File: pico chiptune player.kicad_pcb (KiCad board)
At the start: 2 copper layers, 80 x 70.8 mm, 20 parts, among them J1 MicroSD, J2 Audio Out, SW1 Play / Pause, SW2 Next, SW3 Previous, U1 AY-3-8910, U2 0.96"OLED_I2C

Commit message: Refactor code structure for improved readability and maintainability
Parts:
- added G***: LOGO, LOGO, F.Cu at (120.5, 131.0)
- added G***: LOGO, LOGO, F.Cu at (148.9, 131.0)
- added G***: LOGO, LOGO, F.Cu at (173.0, 112.0)
- added G***: LOGO, LOGO, F.Cu at (177.3, 131.0)
- added G***: LOGO, LOGO, B.Cu at (148.9, 137.2)
- added G***: LOGO, LOGO, B.Cu at (120.2, 137.2)
- added G***: LOGO, LOGO, B.Cu at (177.2, 137.2)
- added R8: 10K, Resistor_SMD:R_0805_2012Metric_Pad1.20x1.40mm_HandSolder, B.Cu at (118.5, 88.5)
- added RV1: 3224W-1-103E, Potentiometer_SMD:Potentiometer_Bourns_3224W_Vertical, B.Cu at (116.5, 104.5)
- added U2: PAM8302AAS, Package_SO:SOIC-8_5.3x5.3mm_P1.27mm, B.Cu at (119.5, 95.0)
- C3: renamed from C4; value 10uF -> 1uF
- J2: value Audio Out -> Spk Out
- JP1: value SEL_TEST2 -> CLK DIV / 2; footprint Jumper:SolderJumper-3_P2.0mm_Open_TrianglePad1.0x1.5mm -> Jumper:SolderJumper-2_P1.3mm_Open_TrianglePad1.0x1.5mm
- R4: renamed from R3; value 1k -> 1K
- R5: renamed from R4; value 1k -> 1K
- R6: renamed from R5; value 1k -> 1K
- U1: value AY-3-8910 -> AY-3-8910 / YM2149F
- moved J2 26.2 mm to (123.5, 100.0), turned to 90 degrees
- moved C3 3.26 mm to (121.5, 83.5)
- moved SW1 2.51 mm to (145.6, 135.0)
- moved SW2 2.51 mm to (174.0, 135.0)
- moved SW3 2.51 mm to (117.2, 135.0)
- moved C2 1.62 mm to (116.0, 88.5), turned to -90 degrees
- moved JP1 0.71 mm to (118.3, 112.7), turned to 180 degrees
- moved C4 0.58 mm to (124.0, 107.5)
- renumbered C3 to C2, C1 to C4, C2 to C5, R7 to R2, R2 to R3, R6 to R7, U2 to U3
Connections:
- C3 pad 2: Net-(J2-Pin_2) -> Net-(C3-Pad2)
- J2 pad 1: GND -> Net-(J2-Pin_1)
- JP1 pad 1: +5V -> Net-(JP1-A)
- JP1 pad 2: Net-(JP1-C) -> GND
- U1 pad 26: Net-(JP1-C) -> Net-(JP1-A)
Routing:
- net Net-(C3-Pad2): track 0.00 -> 24.8 mm
- net +5V: track 163.2 -> 186.9 mm
- net Net-(U2-IN+): track 0.00 -> 11.8 mm
- net Net-(U2-~{SD}): track 0.00 -> 9.46 mm
- net Net-(JP1-C): track 8.24 -> 0.00 mm
- net Net-(JP1-A): track 0.00 -> 7.82 mm
- net Net-(C2-Pad1): track 16.4 -> 10.5 mm
- net Net-(J2-Pin_2): track 5.96 -> 11.8 mm
- net Net-(J2-Pin_1): track 0.00 -> 3.27 mm
- net /SW_PREV: track 36.0 -> 38.7 mm
- net /SW_PLAY: track 38.0 -> 39.6 mm
- net /SW_NEXT: track 51.7 -> 52.5 mm
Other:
- board text added: "+3.3V"
- board text added: "+5V"
- board text added: "/RESET"
- board text added: "A"
- board text added: "B"
- board text added: "C"
- board text added: "CD"
- board text added: "CLK"
- board text added: "CLK/2"
- board text added: "CND"
- board text added: "CS"
- board text added: "D0"
- board text added: "D1"
- board text added: "D2"
- board text added: "D3"
- board text added: "D4"
- board text added: "D5"
- board text added: "D6"
- board text added: "D7"
- board text added: "GND"
- board text added: "MISO"
- board text added: "MOSI"
- board text added: "RP2350 Pico 2 - AY-3-8910"
- board text added: "SCK"
- board text added: "SCL"
- board text added: "SDA"
- board text added: "Terence Ang / MotionFxDesign 2026"
- board text added: "VCC"
- board text added: "VOL"
- board text added: "terenceang.com"

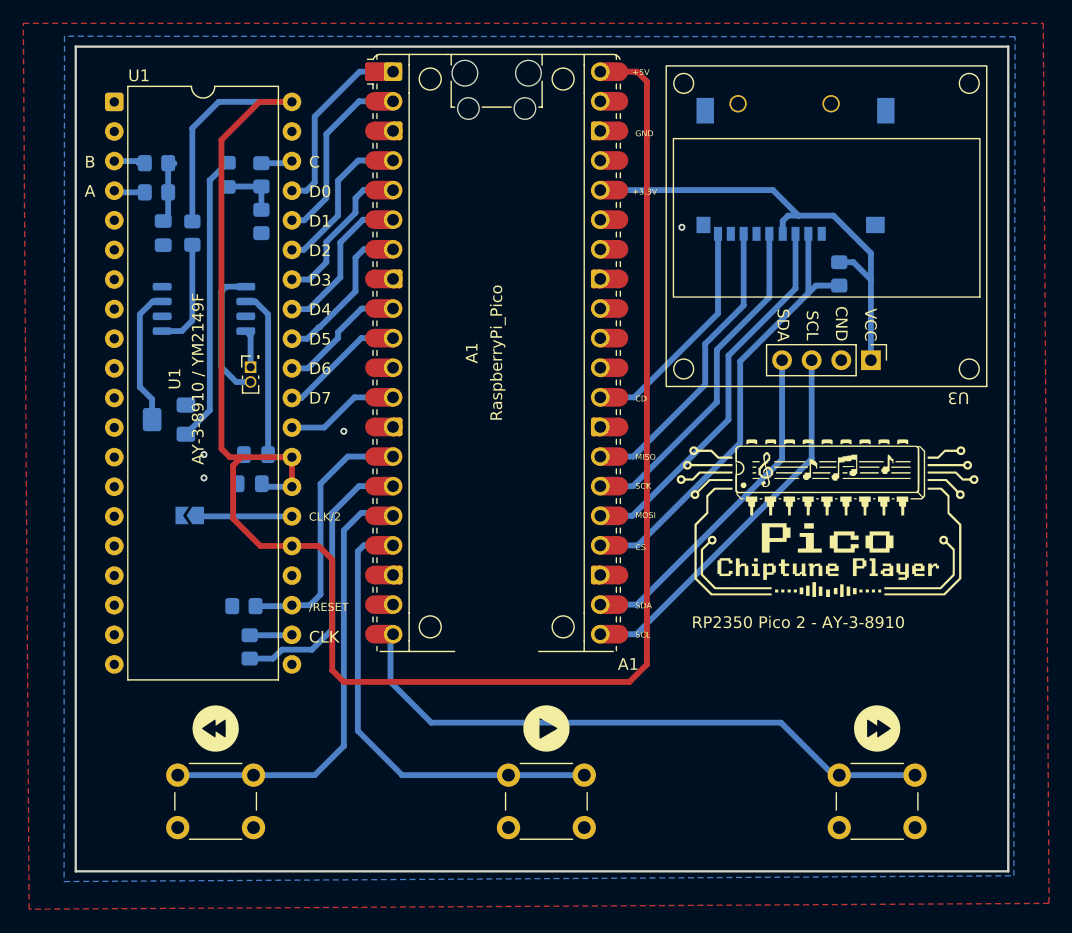
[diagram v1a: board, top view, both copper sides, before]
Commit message: Refactor schematic and project files: Update active layer, modify visible layers, and add polarized capacitor symbol
- Changed active layer from 5 to 2 in the KiCad project file.
- Updated visible layers in the project file for better visibility.
- Removed unused designators and added a new polarized capacitor symbol in the schematic.
- Introduced properties for the new capacitor symbol including reference, value, footprint, and description.
- Cleaned up the schematic by removing the old unpolarized capacitor symbol.
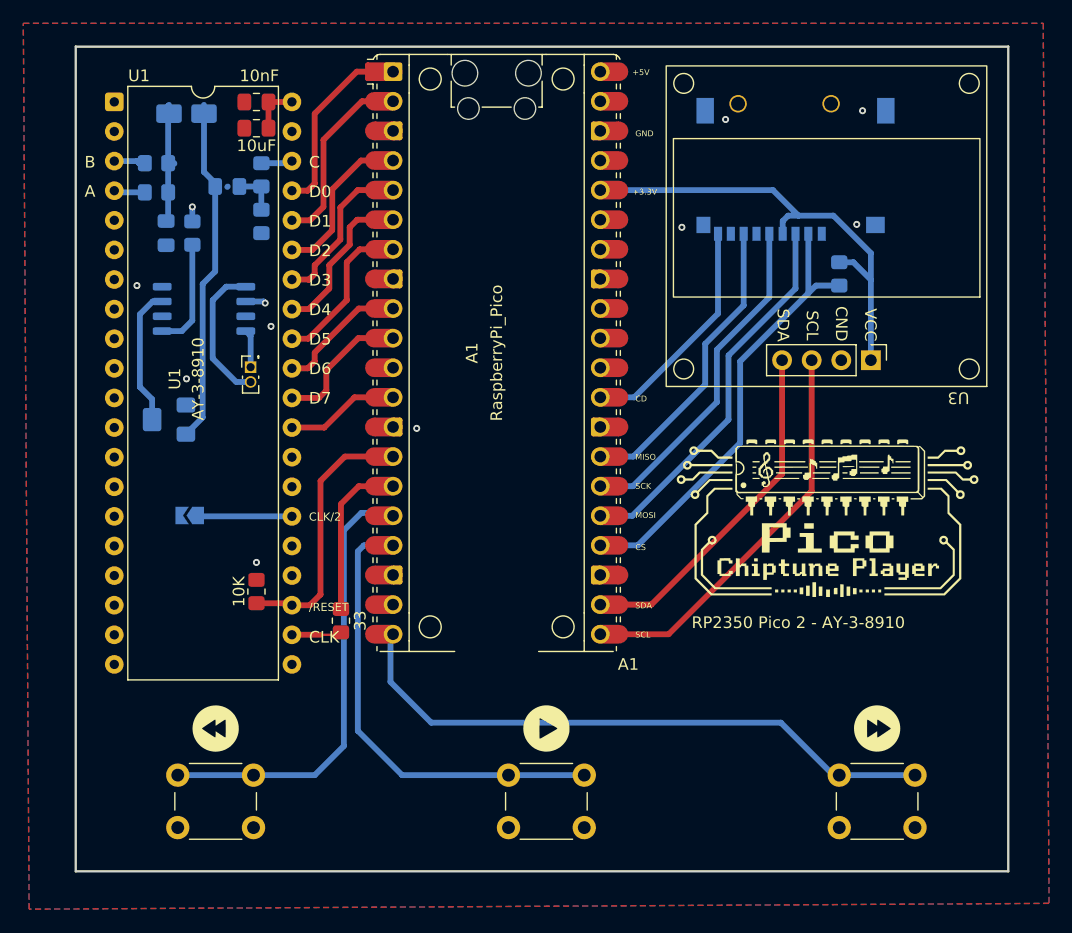
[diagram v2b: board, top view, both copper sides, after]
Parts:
- added C3: 1uF, Capacitor_SMD:CP_Elec_3x5.4, B.Cu at (118.0, 78.2)
- C4, C5, R1, R2: moved to F.Cu
- J2: value Spk Out -> Speaker Out
- JP1: value CLK DIV / 2 -> Clk Div
- R4, R5, R6: value 1K -> 1k
- U1: value AY-3-8910 / YM2149F -> AY-3-8910
- moved C5 32.8 mm to (124.0, 77.2)
- moved C4 28.0 mm to (124.0, 79.5)
- moved R2 8.14 mm to (131.2, 121.8), turned to 90 degrees
- moved R1 1.65 mm to (124.0, 119.2), turned to 90 degrees
- moved C3 1.00 mm to (121.5, 84.5), turned to 180 degrees
- moved C2 0.25 mm to (116.2, 88.5)
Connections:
- U1 pad 24: GND -> +5V
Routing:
- net +5V: track 186.9 -> 7.86 mm, vias 0 -> 5
- net Net-(A1-GPIO11): track 24.3 -> 14.1 mm
- net Net-(C3-Pad2): track 24.8 -> 29.7 mm
- net Net-(C2-Pad1): track 10.5 -> 14.5 mm
- net /OLED_SCL: track 32.8 -> 34.5 mm
- net /CLOCK: track 3.64 -> 4.99 mm
- net /DA7: track 10.8 -> 11.8 mm
- net /OLED_SDA: track 29.3 -> 30.0 mm
- net GND: track 0.63 -> 0.00 mm, vias 4 -> 6
- net Net-(J2-Pin_2): track 11.8 -> 12.4 mm
- added copper zone on In2.Cu, net +5V
- added copper zone on In1.Cu, net GND
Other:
- copper layers 2 -> 4
